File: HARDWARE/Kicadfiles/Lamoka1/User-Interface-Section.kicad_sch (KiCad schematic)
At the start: 25 parts, among them SW1 B3F-4055, U3 74AHCT1G125

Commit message: Get DRC down all the way, other misc improvements
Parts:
- C1, C10, C11, C2, C3, C4, C5, C6, C7, C8, C9, R1, R9: KiLib_Generator (none) -> SMD_2terminal_chip_molded
- U3: KiLib_Generator (none) -> package/gullwing
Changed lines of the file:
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@@
 			)
 		)
+		(property "KiLib_Generator" "SMD_2terminal_chip_molded"
+			(at 118.11 152.4 0)
+			(hide yes)
+			(show_name no)
+			(do_not_autoplace no)
+			(effects
+				(font
+					(size 1.27 1.27)
+				)
+			)
+		)
 		(pin "1"
 		)
@@
 			)
 		)
+		(property "KiLib_Generator" "SMD_2terminal_chip_molded"
+			(at 72.39 152.4 0)
+			(hide yes)
+			(show_name no)
+			(do_not_autoplace no)
+			(effects
+				(font
+					(size 1.27 1.27)
+				)
+			)
+		)
 		(pin "1"
 		)
@@
 			)
 		)
+		(property "KiLib_Generator" "SMD_2terminal_chip_molded"
+			(at 60.96 152.4 0)
+			(hide yes)
+			(show_name no)
+			(do_not_autoplace no)
+			(effects
+				(font
+					(size 1.27 1.27)
+				)
+			)
+		)
 		(pin "1"
 		)
@@
 			)
 		)
+		(property "KiLib_Generator" "SMD_2terminal_chip_molded"
+			(at 106.68 152.4 0)
+			(hide yes)
+			(show_name no)
+			(do_not_autoplace no)
+			(effects
+				(font
+					(size 1.27 1.27)
+				)
+			)
+		)
 		(pin "1"
 		)
@@
 			)
 		)
+		(property "KiLib_Generator" "SMD_2terminal_chip_molded"
+			(at 140.97 152.4 0)
+			(hide yes)
+			(show_name no)
+			(do_not_autoplace no)
+			(effects
+				(font
+					(size 1.27 1.27)
+				)
+			)
+		)
 		(pin "1"
 		)
@@
 			)
 		)
+		(property "KiLib_Generator" "SMD_2terminal_chip_molded"
+			(at 49.53 152.4 0)
+			(hide yes)
+			(show_name no)
+			(do_not_autoplace no)
+			(effects
+				(font
+					(size 1.27 1.27)
+				)
+			)
+		)
 		(pin "1"
 		)
@@
 			)
 		)
+		(property "KiLib_Generator" "SMD_2terminal_chip_molded"
+			(at 55.88 172.72 0)
+			(hide yes)
+			(show_name no)
+			(do_not_autoplace no)
+			(effects
+				(font
+					(size 1.27 1.27)
+				)
+			)
+		)
 		(pin "1"
 		)
@@
 			)
 		)
+		(property "KiLib_Generator" "SMD_2terminal_chip_molded"
+			(at 152.4 152.4 0)
+			(hide yes)
+			(show_name no)
+			(do_not_autoplace no)
+			(effects
+				(font
+					(size 1.27 1.27)
+				)
+			)
+		)
 		(pin "1"
 		)
@@
 			)
 		)
+		(property "KiLib_Generator" "SMD_2terminal_chip_molded"
+			(at 129.54 152.4 0)
+			(hide yes)
+			(show_name no)
+			(do_not_autoplace no)
+			(effects
+				(font
+					(size 1.27 1.27)
+				)
+			)
+		)
 		(pin "1"
 		)
@@
 			)
 		)
+		(property "KiLib_Generator" "package/gullwing"
+			(at 41.91 106.68 0)
+			(hide yes)
+			(show_name no)
+			(do_not_autoplace no)
+			(effects
+				(font
+					(size 1.27 1.27)
+				)
+			)
+		)
 		(pin "3"
 		)
@@
 			)
 		)
+		(property "KiLib_Generator" "SMD_2terminal_chip_molded"
+			(at 95.25 152.4 0)
+			(hide yes)
+			(show_name no)
+			(do_not_autoplace no)
+			(effects
+				(font
+					(size 1.27 1.27)
+				)
+			)
+		)
 		(pin "1"
 		)
@@
 			)
 		)
+		(property "KiLib_Generator" "SMD_2terminal_chip_molded"
+			(at 53.34 49.53 0)
+			(hide yes)
+			(show_name no)
+			(do_not_autoplace no)
+			(effects
+				(font
+					(size 1.27 1.27)
+				)
+			)
+		)
 		(pin "2"
 		)
@@
 			)
 		)
+		(property "KiLib_Generator" "SMD_2terminal_chip_molded"
+			(at 83.82 152.4 0)
+			(hide yes)
+			(show_name no)
+			(do_not_autoplace no)
+			(effects
+				(font
+					(size 1.27 1.27)
+				)
+			)
+		)
 		(pin "1"
 		)
@@
 			(hide yes)
 			(show_name no)
+			(do_not_autoplace no)
+			(effects
+				(font
+					(size 1.27 1.27)
+				)
+			)
+		)
+		(property "KiLib_Generator" "SMD_2terminal_chip_molded"
+			(at 64.77 119.38 0)
+			(hide yes)
+			(show_name no)

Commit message: misc fixes
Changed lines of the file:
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@@
+	)
+	(symbol
+		(lib_id "power:PWR_FLAG")
+		(at 81.28 111.76 0)
+		(unit 1)
+		(body_style 1)
+		(exclude_from_sim no)
+		(in_bom yes)
+		(on_board yes)
+		(in_pos_files yes)
+		(dnp no)
+		(fields_autoplaced yes)
+		(property "Reference" "#FLG14"
+			(at 81.28 111.76 0)
+			(hide yes)
+			(show_name no)
+			(do_not_autoplace no)
+			(effects
+				(font
+					(size 1.27 1.27)
+				)
+			)
+		)
+		(property "Value" "PWR_FLAG"
+			(at 81.28 111.76 0)
+			(hide yes)
+			(show_name no)
+			(do_not_autoplace no)
+			(effects
+				(font
+					(size 1.27 1.27)
+				)
+			)
+		)
+		(property "Footprint" ""
+			(at 81.28 111.76 0)
+			(hide yes)
+			(show_name no)
+			(do_not_autoplace no)
+			(effects
+				(font
+					(size 1.27 1.27)
+				)
+			)
+		)
+		(property "Datasheet" ""
+			(at 81.28 111.76 0)
+			(hide yes)
+			(show_name no)
+			(do_not_autoplace no)
+			(effects
+				(font
+					(size 1.27 1.27)
+				)
+			)
+		)
+		(property "Description" "Special symbol for telling ERC where power comes from"
+			(at 81.28 111.76 0)
+			(hide yes)
+			(show_name no)
+			(do_not_autoplace no)
+			(effects
+				(font
+					(size 1.27 1.27)
+				)
+			)
+		)
+		(pin "1"
+		)
+		(instances
+			(project "Lamoka1"
+				(path "/c7bb62b6-932f-49c1-a356-0286e905fc0a/e6907476-b7b0-4897-94b6-ac3817b6fb94"
+					(reference "#FLG14")
+					(unit 1)
+				)
+			)
+		)
 	)
 	(symbol

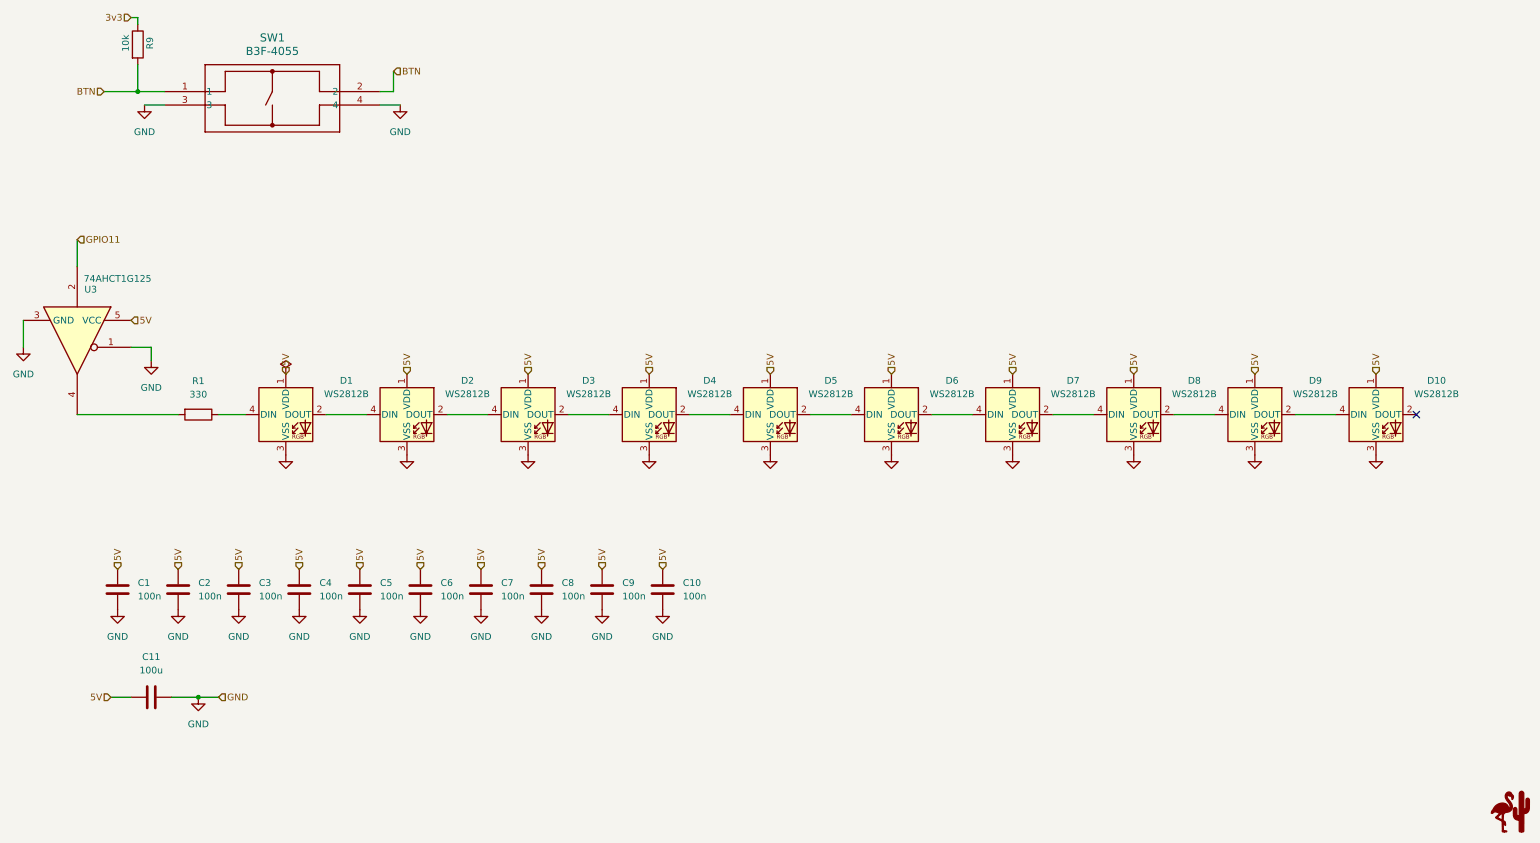
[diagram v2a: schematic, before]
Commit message: major reform on the size of the Lamoka1/2
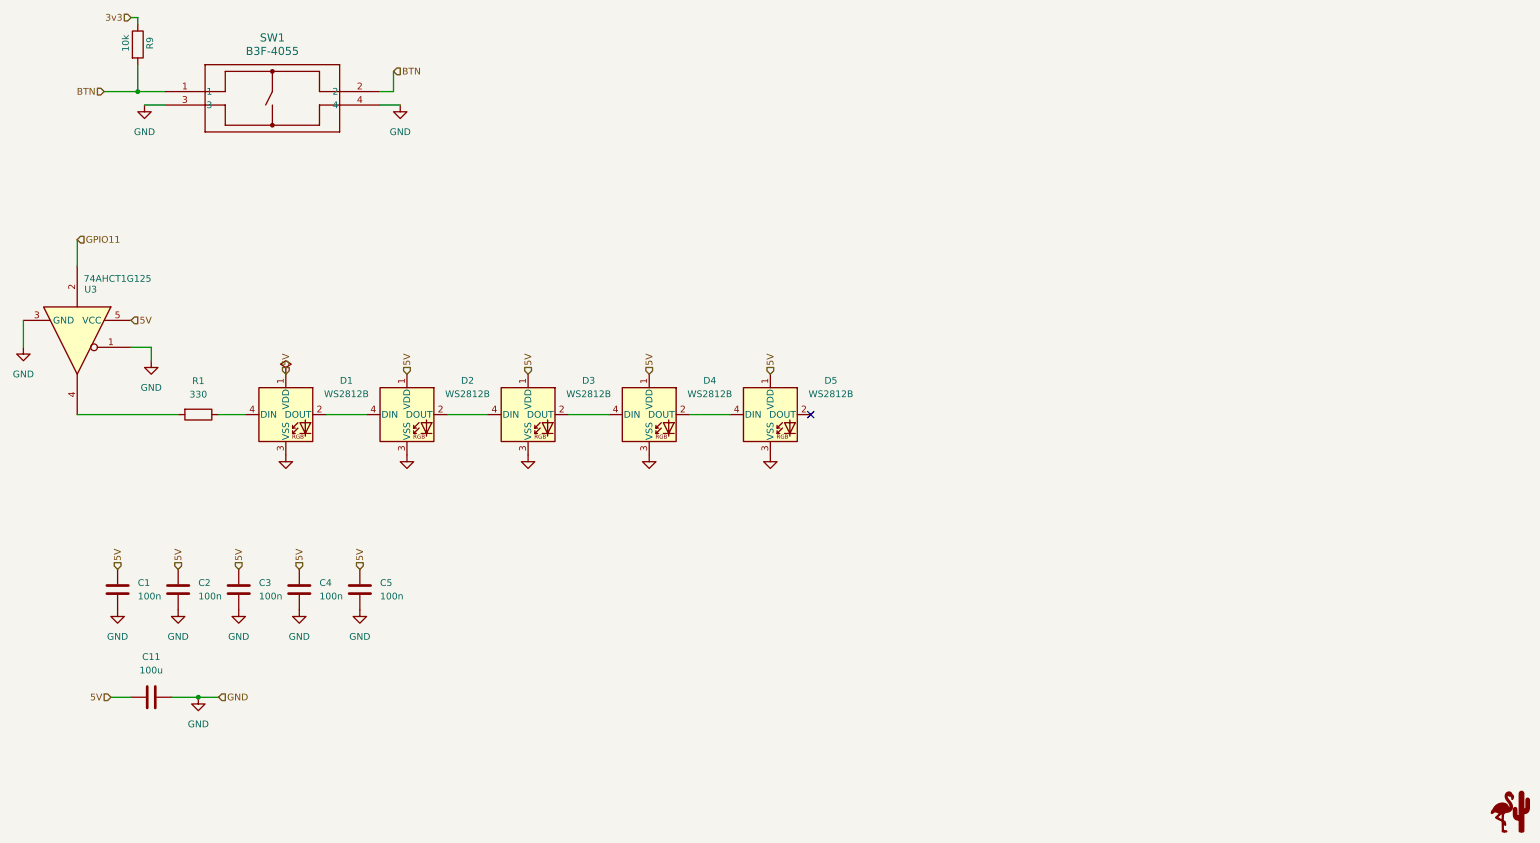
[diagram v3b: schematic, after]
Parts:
- removed C10, C6, C7, C8, C9: 100n, Capacitor_SMD:C_0603_1608Metric, symbol Device:C
- removed D10, D6, D7, D8, D9: WS2812B, LED_SMD:LED_WS2812B_PLCC4_5.0x5.0mm_P3.2mm, symbol LED:WS2812B
- C1, C2, C3, C4, C5: MPN CL05B104KO5NNNC -> CL10B104KO8NNNC

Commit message: finishing up routing and all of the lamoka1/2
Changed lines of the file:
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@@
-	)
-	(symbol
-		(lib_id "power:PWR_FLAG")
-		(at 81.28 111.76 0)
-		(unit 1)
-		(body_style 1)
-		(exclude_from_sim no)
-		(in_bom yes)
-		(on_board yes)
-		(in_pos_files yes)
-		(dnp no)
-		(fields_autoplaced yes)
-		(property "Reference" "#FLG14"
-			(at 81.28 111.76 0)
-			(hide yes)
-			(show_name no)
-			(do_not_autoplace no)
-			(effects
-				(font
-					(size 1.27 1.27)
-				)
-			)
-		)
-		(property "Value" "PWR_FLAG"
-			(at 81.28 111.76 0)
-			(hide yes)
-			(show_name no)
-			(do_not_autoplace no)
-			(effects
-				(font
-					(size 1.27 1.27)
-				)
-			)
-		)
-		(property "Footprint" ""
-			(at 81.28 111.76 0)
-			(hide yes)
-			(show_name no)
-			(do_not_autoplace no)
-			(effects
-				(font
-					(size 1.27 1.27)
-				)
-			)
-		)
-		(property "Datasheet" ""
-			(at 81.28 111.76 0)
-			(hide yes)
-			(show_name no)
-			(do_not_autoplace no)
-			(effects
-				(font
-					(size 1.27 1.27)
-				)
-			)
-		)
-		(property "Description" "Special symbol for telling ERC where power comes from"
-			(at 81.28 111.76 0)
-			(hide yes)
-			(show_name no)
-			(do_not_autoplace no)
-			(effects
-				(font
-					(size 1.27 1.27)
-				)
-			)
-		)
-		(pin "1"
-		)
-		(instances
-			(project "Lamoka1"
-				(path "/c7bb62b6-932f-49c1-a356-0286e905fc0a/e6907476-b7b0-4897-94b6-ac3817b6fb94"
-					(reference "#FLG14")
-					(unit 1)
-				)
-			)
-		)
 	)
 	(symbol
